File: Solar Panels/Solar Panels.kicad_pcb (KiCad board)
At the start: 2 copper layers, 113 x 82 mm, 98 parts, among them J2 5040500891

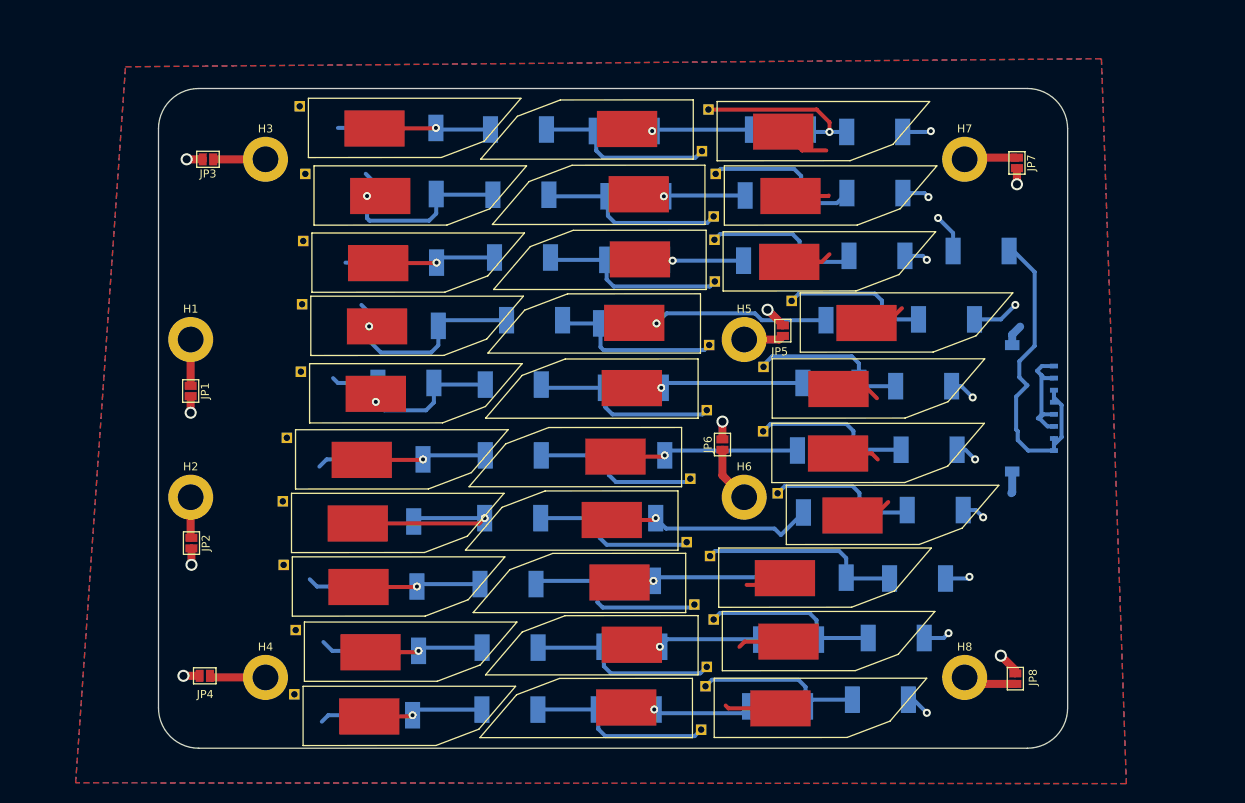
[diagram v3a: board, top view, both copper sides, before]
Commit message: Diodes changes and adjusted schematic.
Made the diode changes based off Parker's suggestions and fixed the schematic. Comments are now included within the schematic.
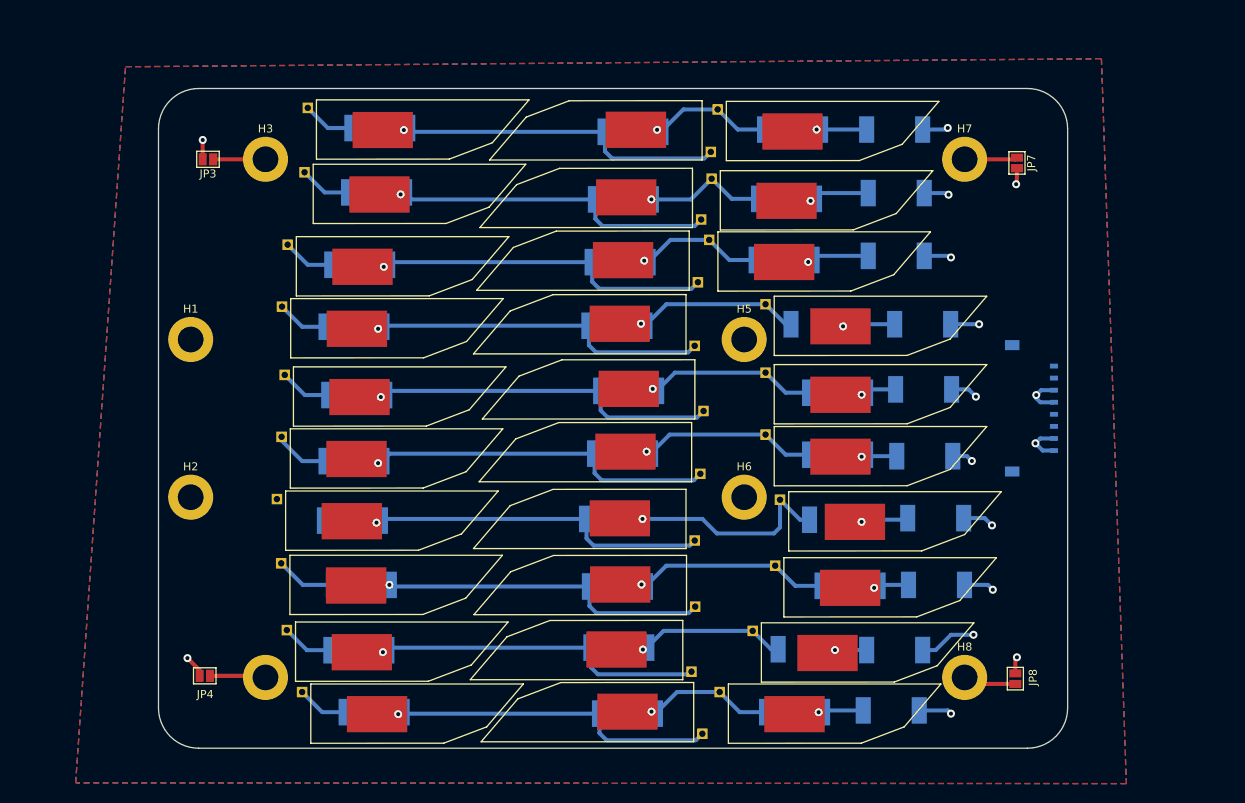
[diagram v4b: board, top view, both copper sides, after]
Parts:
- removed CR41, CR42, CR43, CR44, CR45, CR46, CR47, CR48, CR49, CR50, CR51: S3B_R1_00001, Solar Panel Library:SMC&slash_DO-214AB_PNJ
- removed JP1, JP2, JP5, JP6: Jumper_2_Open, Jumper:SolderJumper-2_P1.3mm_Open_Pad1.0x1.5mm
- H1, H2, H5, H6: value MountingHole_Pad -> MountingHole
- moved CR32 71.9 mm to (100.2, 136.7)
- moved CR16 65.6 mm to (99.3, 104.6)
- moved CR8 61.9 mm to (102.1, 87.9)
- moved CR28 59.4 mm to (99.1, 128.7)
- moved CR26 56.3 mm to (159.4, 128.6)
- moved CR25 55.1 mm to (171.6, 128.4)
- moved CR13 50.4 mm to (170.0, 104.3)
- moved CR30 44.9 mm to (161.0, 136.8)
- moved CR29 40.6 mm to (171.7, 136.7)
- moved CR27 40.0 mm to (131.7, 128.5)
- moved CR24 35.9 mm to (99.3, 121.3)
- moved CR5 34.4 mm to (153.1, 88.7)
- moved CR10 33.7 mm to (152.8, 96.3)
- moved CR9 33.2 mm to (166.7, 95.8)
- moved CR31 31.8 mm to (132.0, 136.9)
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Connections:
- CR10 pad 1: Net-(SC5--) -> Net-(SC7-+)
- CR10 pad 2: Net-(SC6-+) -> Net-(SC7--)
- CR11 pad 1: Net-(SC6-+) -> Net-(SC7--)
- CR11 pad 2: GND -> Net-(SC8--)
- CR12 pad 1: Net-(SC9-+) -> Net-(SC8--)
- CR13 pad 1: Net-(SC8--) -> +VDC
- CR13 pad 2: Net-(SC9-+) -> Net-(SC10-+)
- CR14 pad 1: Net-(SC8-+) -> Net-(SC10-+)
- CR14 pad 2: Net-(SC8--) -> Net-(SC10--)
- CR15 pad 1: Net-(SC7--) -> Net-(SC10--)
- CR15 pad 2: Net-(SC8-+) -> Net-(SC11--)
- CR16 pad 1: Net-(SC1-+) -> Net-(SC11--)
- CR16 pad 2: Net-(SC7--) -> GND
- CR17 pad 1: Net-(SC10--) -> +VDC
- CR17 pad 2: Net-(SC11-+) -> Net-(SC13-+)
- CR18 pad 1: Net-(SC11-+) -> Net-(SC13-+)
- CR18 pad 2: Net-(SC11--) -> Net-(SC13--)
- CR19 pad 1: Net-(SC11--) -> Net-(SC13--)
- CR19 pad 2: Net-(SC12-+) -> Net-(SC14--)
- CR20 pad 1: Net-(SC12-+) -> Net-(SC14--)
- CR21 pad 1: Net-(SC1-+) -> +VDC
- CR21 pad 2: Net-(SC10--) -> Net-(SC16-+)
- CR22 pad 1: Net-(SC1-+) -> Net-(SC16-+)
- CR22 pad 2: Net-(SC13--) -> Net-(SC16--)
- CR23 pad 1: Net-(SC13--) -> Net-(SC16--)
- CR23 pad 2: Net-(SC14-+) -> Net-(SC17--)
- CR24 pad 1: Net-(SC14-+) -> Net-(SC17--)
- CR24 pad 2: Net-(SC14--) -> GND
- CR25 pad 1: Net-(SC14--) -> +VDC
- CR25 pad 2: Net-(SC15-+) -> Net-(SC19-+)
- CR26 pad 1: Net-(SC15-+) -> Net-(SC19-+)
- CR26 pad 2: GND -> Net-(SC19--)
- CR27 pad 1: Net-(SC1-+) -> Net-(SC19--)
- CR27 pad 2: Net-(SC16--) -> Net-(SC20--)
- CR28 pad 1: Net-(SC16--) -> Net-(SC20--)
- CR28 pad 2: Net-(SC17-+) -> GND
- CR29 pad 1: Net-(SC17-+) -> +VDC
- CR29 pad 2: Net-(SC17--) -> Net-(SC22-+)
- CR3 pad 1: Net-(SC1--) -> +VDC
- CR3 pad 2: Net-(SC2-+) -> Net-(SC4-+)
- CR30 pad 1: Net-(SC17--) -> Net-(SC22-+)
- CR30 pad 2: Net-(SC18-+) -> Net-(SC22--)
- CR31 pad 1: Net-(SC18-+) -> Net-(SC22--)
- CR31 pad 2: GND -> Net-(SC23--)
- CR32 pad 1: Net-(SC1-+) -> Net-(SC23--)
- CR32 pad 2: Net-(SC19--) -> GND
- CR33 pad 1: Net-(SC19--) -> +VDC
- CR33 pad 2: Net-(SC20-+) -> Net-(SC25-+)
- CR34 pad 1: Net-(SC20-+) -> Net-(SC25-+)
- CR34 pad 2: Net-(SC20--) -> Net-(SC25--)
- CR35 pad 1: Net-(SC20--) -> Net-(SC25--)
- CR35 pad 2: Net-(SC21-+) -> Net-(SC26--)
- CR36 pad 1: Net-(SC21-+) -> Net-(SC26--)
- CR37 pad 1: Net-(SC1-+) -> +VDC
- CR37 pad 2: Net-(SC22--) -> Net-(SC28-+)
- CR38 pad 1: Net-(SC22--) -> Net-(SC28-+)
- CR38 pad 2: Net-(SC23-+) -> Net-(SC28--)
- CR39 pad 1: Net-(SC23-+) -> Net-(SC28--)
- CR39 pad 2: Net-(SC23--) -> Net-(SC29--)
- CR4 pad 1: Net-(SC2-+) -> Net-(SC1--)
- CR40 pad 1: Net-(SC23--) -> Net-(SC29--)
- CR40 pad 2: Net-(SC24-+) -> GND
- CR5 pad 1: Net-(SC2--) -> Net-(SC4-+)
- CR5 pad 2: Net-(SC3-+) -> Net-(SC4--)
- CR6 pad 1: Net-(SC3-+) -> Net-(SC2--)
- CR7 pad 2: Net-(SC5-+) -> Net-(SC5--)
- CR8 pad 1: Net-(SC1-+) -> Net-(SC5--)
- CR8 pad 2: Net-(SC4--) -> GND
- CR9 pad 1: Net-(SC5-+) -> +VDC
- CR9 pad 2: Net-(SC5--) -> Net-(SC7-+)
- H1 pad 1: Net-(JP1-A) -> (no net)
- H2 pad 1: Net-(JP2-A) -> (no net)
- H5 pad 1: Net-(JP5-A) -> (no net)
- H6 pad 1: Net-(JP6-A) -> (no net)
- SC10 pad 1: Net-(SC1-+) -> Net-(SC10-+)
- SC11 pad 1: Net-(SC11-+) -> Net-(SC10--)
- SC12 pad 1: Net-(SC12-+) -> Net-(SC11--)
- SC13 pad 1: Net-(SC1-+) -> Net-(SC13-+)
- SC14 pad 1: Net-(SC14-+) -> Net-(SC13--)
- SC15 pad 1: Net-(SC15-+) -> Net-(SC14--)
- SC16 pad 1: Net-(SC1-+) -> Net-(SC16-+)
- SC17 pad 1: Net-(SC17-+) -> Net-(SC16--)
- SC18 pad 1: Net-(SC18-+) -> Net-(SC17--)
- SC19 pad 1: Net-(SC1-+) -> Net-(SC19-+)
- SC2 pad 1: Net-(SC2-+) -> Net-(SC1--)
- SC20 pad 1: Net-(SC20-+) -> Net-(SC19--)
- SC21 pad 1: Net-(SC21-+) -> Net-(SC20--)
- SC22 pad 1: Net-(SC1-+) -> Net-(SC22-+)
- SC23 pad 1: Net-(SC23-+) -> Net-(SC22--)
- SC24 pad 1: Net-(SC24-+) -> Net-(SC23--)
- SC25 pad 1: Net-(SC1-+) -> Net-(SC25-+)
- SC26 pad 1: Net-(SC26-+) -> Net-(SC25--)
- SC27 pad 1: Net-(SC27-+) -> Net-(SC26--)
- SC28 pad 1: Net-(SC1-+) -> Net-(SC28-+)
- SC29 pad 1: Net-(SC29-+) -> Net-(SC28--)
- SC3 pad 1: Net-(SC3-+) -> Net-(SC2--)
- SC30 pad 1: Net-(SC30-+) -> Net-(SC29--)
- SC4 pad 1: Net-(SC1-+) -> Net-(SC4-+)
- SC5 pad 1: Net-(SC5-+) -> Net-(SC4--)
- SC6 pad 1: Net-(SC6-+) -> Net-(SC5--)
- SC7 pad 1: Net-(SC1-+) -> Net-(SC7-+)
- SC8 pad 1: Net-(SC8-+) -> Net-(SC7--)
- SC9 pad 1: Net-(SC9-+) -> Net-(SC8--)
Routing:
- net Net-(SC1-+): track 94.5 -> 6.22 mm, vias 11 -> 1
- net Net-(SC20-+): track 26.0 -> 0.00 mm, vias 1 -> 0
- net Net-(SC21-+): track 25.0 -> 0.00 mm, vias 1 -> 0
- net Net-(SC11-+): track 24.7 -> 0.00 mm, vias 1 -> 0
- net Net-(SC17-+): track 22.9 -> 0.00 mm, vias 1 -> 0
- net Net-(SC12-+): track 22.6 -> 0.00 mm, vias 1 -> 0
- net Net-(SC23--): track 22.9 -> 45.4 mm, vias 0 -> 1
- net Net-(SC17--): track 21.5 -> 43.7 mm, vias 0 -> 1
- net Net-(SC20--): track 21.1 -> 42.8 mm, vias 0 -> 1
- net Net-(SC14-+): track 21.5 -> 0.00 mm, vias 1 -> 0
- net Net-(SC23-+): track 21.5 -> 0.00 mm, vias 1 -> 0
- net Net-(SC6-+): track 21.4 -> 0.00 mm, vias 1 -> 0
- net Net-(SC11--): track 21.7 -> 42.6 mm, vias 0 -> 1
- net Net-(SC14--): track 23.7 -> 43.6 mm, vias 0 -> 1
- net Net-(SC2--): track 22.5 -> 41.6 mm, vias 0 -> 1
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- added copper zone on F.Cu, net +VDC
- removed copper zone on F.Cu, net Net-(SC1-+)

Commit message: Quick Adjustments to Schematic and Routing
Adjusted so there's only one bypass diode for the entire panel. Made changes to the routing as well.
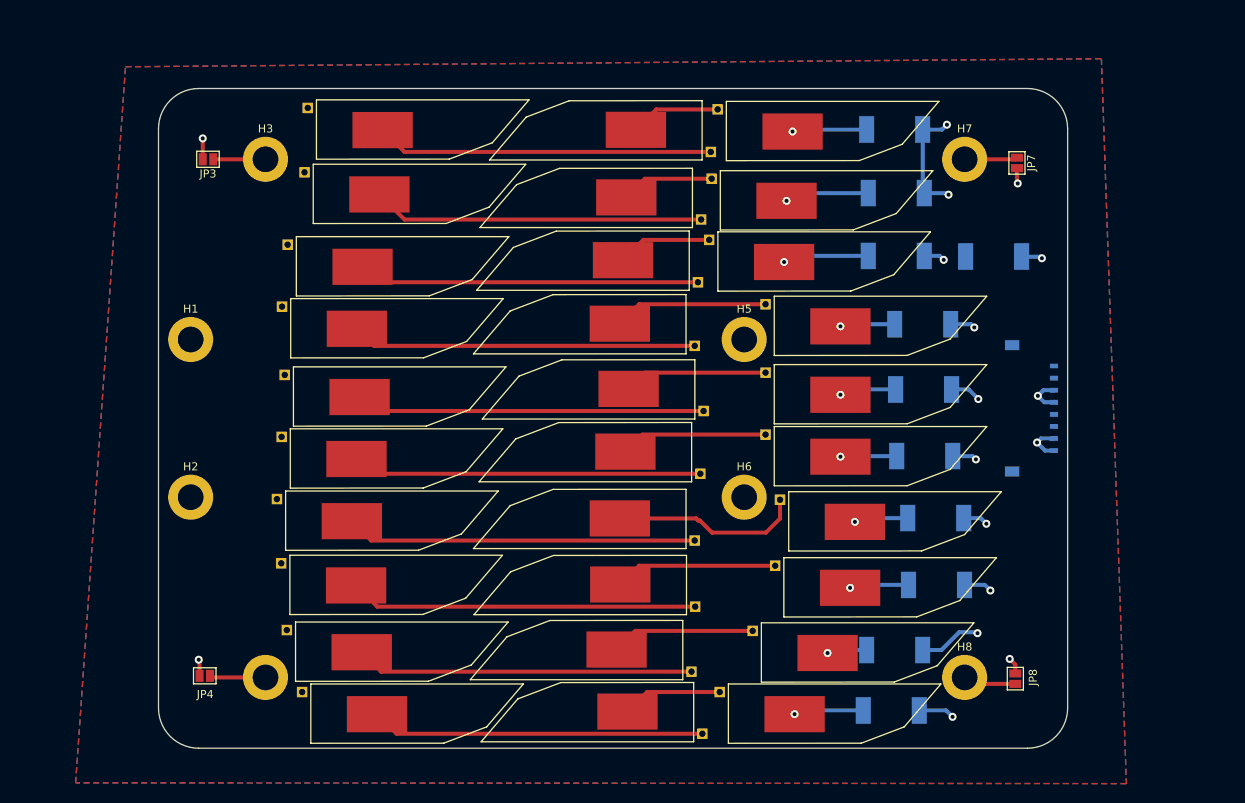
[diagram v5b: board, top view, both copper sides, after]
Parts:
- removed CR10, CR11, CR12, CR14, CR15, CR16, CR18, CR19, CR20, CR22, CR23, CR24, CR26, CR27, CR28, CR30, CR31, CR32, CR34, CR35, CR36, CR38, CR39, CR4, CR40, CR5, CR6, CR7, CR8: S3B_R1_00001, Solar Panel Library:SMC&slash_DO-214AB_PNJ
- moved CR2 29.6 mm to (178.8, 95.9)
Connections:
- CR2 pad 1: Net-(SC1-+) -> +VDC
- CR2 pad 2: Net-(SC1--) -> GND
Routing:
- net GND: track 69.0 -> 8.67 mm
- net +VDC: track 48.8 -> 57.9 mm, vias 12 -> 13
- net Net-(SC4--): track 18.6 -> 11.6 mm, vias 1 -> 0
- net Net-(SC7--): track 18.3 -> 11.8 mm, vias 1 -> 0
- net Net-(SC19--): track 29.1 -> 23.7 mm, vias 1 -> 0
- net Net-(SC22--): track 24.7 -> 20.2 mm, vias 1 -> 0
- net Net-(SC1--): track 15.7 -> 11.2 mm, vias 1 -> 0
- net Net-(SC16--): track 22.4 -> 18.3 mm, vias 1 -> 0
- net Net-(SC28--): track 16.6 -> 12.5 mm, vias 1 -> 0
- net Net-(SC13--): track 21.6 -> 17.9 mm, vias 1 -> 0
- net Net-(SC1-+): track 6.22 -> 9.31 mm
- net Net-(SC28-+): track 5.64 -> 8.73 mm
- net Net-(SC7-+): track 7.79 -> 10.8 mm
- net Net-(SC22-+): track 4.42 -> 7.41 mm
- net Net-(SC4-+): track 7.57 -> 10.6 mm
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
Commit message: Routed the PCB after the Footprint Adjustments
Routed the PCB after making adjustments to the TriSolX footprint.
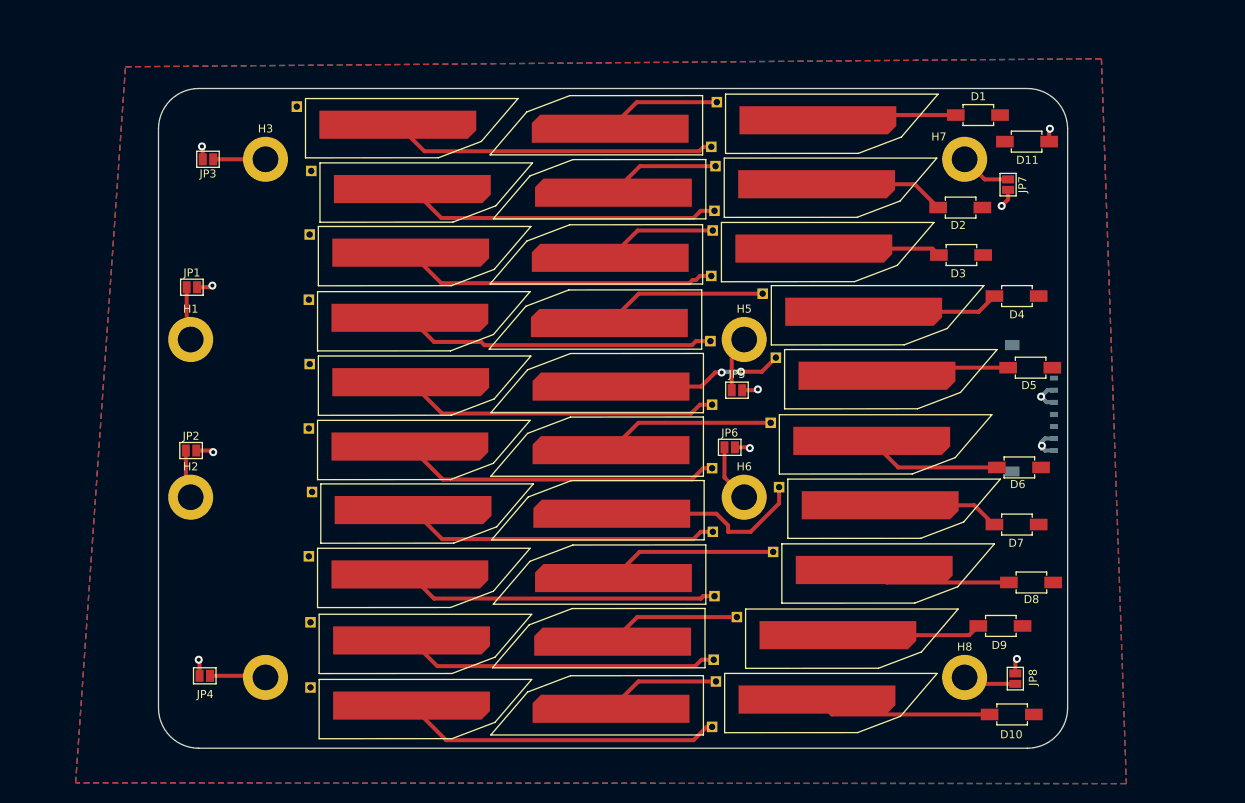
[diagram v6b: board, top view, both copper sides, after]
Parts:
- removed CR1, CR13, CR17, CR2, CR21, CR25, CR29, CR3, CR33, CR37, CR9: S3B_R1_00001, Solar Panel Library:SMC&slash_DO-214AB_PNJ
- added D1: PMEG10020AELPX, Solar Panel Library:PMEG10020AELPX, F.Cu at (176.9, 78.3)
- added D10: PMEG10020AELPX, Solar Panel Library:PMEG10020AELPX, F.Cu at (181.1, 152.8)
- added D11: PMEG10020AELPX, Solar Panel Library:PMEG10020AELPX, F.Cu at (182.9, 81.6)
- added D2: PMEG10020AELPX, Solar Panel Library:PMEG10020AELPX, F.Cu at (174.7, 89.8)
- added D3: PMEG10020AELPX, Solar Panel Library:PMEG10020AELPX, F.Cu at (174.8, 95.7)
- added D4: PMEG10020AELPX, Solar Panel Library:PMEG10020AELPX, F.Cu at (181.7, 100.8)
- added D5: PMEG10020AELPX, Solar Panel Library:PMEG10020AELPX, F.Cu at (183.4, 109.7)
- added D6: PMEG10020AELPX, Solar Panel Library:PMEG10020AELPX, F.Cu at (182.0, 122.1)
- added D7: PMEG10020AELPX, Solar Panel Library:PMEG10020AELPX, F.Cu at (181.7, 129.2)
- added D8: PMEG10020AELPX, Solar Panel Library:PMEG10020AELPX, F.Cu at (183.5, 136.4)
- added D9: PMEG10020AELPX, Solar Panel Library:PMEG10020AELPX, F.Cu at (179.7, 141.8)
- added JP1: Jumper_2_Open, Jumper:SolderJumper-2_P1.3mm_Open_Pad1.0x1.5mm, F.Cu at (79.2, 99.7)
- added JP2: Jumper_2_Open, Jumper:SolderJumper-2_P1.3mm_Open_Pad1.0x1.5mm, F.Cu at (79.0, 120.0)
- added JP5: Jumper_2_Open, Jumper:SolderJumper-2_P1.3mm_Open_Pad1.0x1.5mm, F.Cu at (146.9, 112.5)
- added JP6: Jumper_2_Open, Jumper:SolderJumper-2_P1.3mm_Open_Pad1.0x1.5mm, F.Cu at (146.0, 119.6)
- H1, H2, H5, H6: value MountingHole -> MountingHole_Pad
- moved SC21 4.46 mm to (103.4, 127.7)
- moved SC18 3.55 mm to (103.0, 119.8)
- moved SC24 3.55 mm to (103.0, 135.7)
- moved SC12 3.45 mm to (103.0, 103.8)
- moved SC15 3.38 mm to (103.1, 111.8)
- moved SC26 3.14 mm to (134.7, 143.5)
- moved SC27 3.09 mm to (103.2, 143.8)
- moved SC9 3.02 mm to (103.1, 95.7)
- moved JP7 2.92 mm to (180.6, 87.0)
- moved SC23 2.73 mm to (134.8, 135.6)
- moved SC25 2.61 mm to (156.2, 143.2)
- moved SC20 2.50 mm to (134.6, 127.6)
- moved SC13 2.27 mm to (161.1, 111.0)
- moved SC11 2.04 mm to (134.3, 103.9)
- moved SC5 1.98 mm to (134.8, 87.7)
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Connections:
- H1 pad 1: (no net) -> Net-(JP1-A)
- H2 pad 1: (no net) -> Net-(JP2-A)
- H5 pad 1: (no net) -> Net-(JP5-A)
- H6 pad 1: (no net) -> Net-(JP6-A)
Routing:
- net +VDC: track 57.9 -> 8.05 mm, vias 13 -> 2
- net Net-(SC28-+): track 8.73 -> 22.2 mm, vias 1 -> 0
- net Net-(SC25-+): track 5.01 -> 17.9 mm, vias 1 -> 0
- net Net-(SC10-+): track 6.85 -> 17.1 mm, vias 1 -> 0
- net Net-(SC22-+): track 7.41 -> 17.4 mm, vias 1 -> 0
- net Net-(SC16-+): track 7.03 -> 16.9 mm, vias 1 -> 0
- net Net-(SC13-+): track 7.13 -> 16.7 mm, vias 1 -> 0
- net GND: track 8.67 -> 17.6 mm, vias 4 -> 9
- net Net-(SC19-+): track 6.75 -> 15.2 mm, vias 1 -> 0
- net Net-(SC1-+): track 9.31 -> 17.4 mm, vias 1 -> 0
- net Net-(JP6-A): track 0.00 -> 7.21 mm
- net Net-(JP5-A): track 0.00 -> 6.94 mm
- net Net-(JP1-A): track 0.00 -> 6.71 mm
- net Net-(JP2-A): track 0.00 -> 6.05 mm
- net Net-(SC4-+): track 10.6 -> 16.3 mm, vias 1 -> 0
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
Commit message: Refined Simons 2u
I tried refining Simons design a bit and aligned the holes/dimensions to the most current frame version.

Looking good on the structural side. Think we just need a last electrical review then should be ready to order.
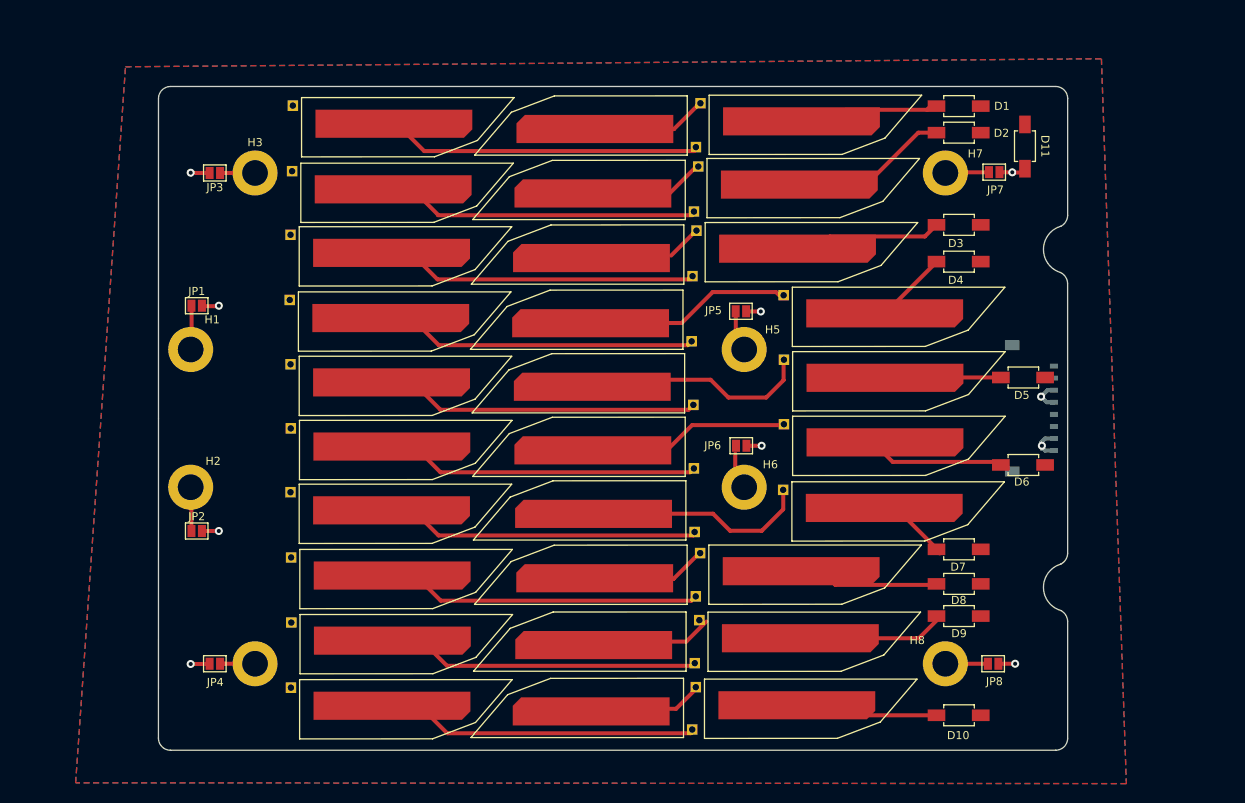
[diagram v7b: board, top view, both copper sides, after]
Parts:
- moved JP2 10.0 mm to (79.8, 130.0)
- moved JP5 9.82 mm to (147.4, 102.7)
- moved D2 9.31 mm to (174.5, 80.5)
- moved SC22 9.08 mm to (151.6, 135.2)
- moved D8 9.00 mm to (174.5, 136.6)
- moved D4 8.38 mm to (174.5, 96.5)
- moved D7 7.83 mm to (174.5, 132.3)
- moved D10 6.60 mm to (174.5, 152.9)
- moved D9 5.34 mm to (174.5, 140.6)
- moved SC25 4.68 mm to (151.5, 143.6)
- moved D3 3.77 mm to (174.5, 91.9)
- moved JP8 3.32 mm to (178.7, 146.5), turned to 0 degrees
- moved H7 2.94 mm to (172.8, 85.5)
- moved H8 2.94 mm to (172.8, 146.5)
- moved SC21 2.69 mm to (100.7, 127.7)
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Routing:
- net Net-(SC28-+): track 22.2 -> 10.9 mm
- net Net-(SC7--): track 14.1 -> 4.37 mm
- net Net-(SC4--): track 14.1 -> 4.82 mm
- net Net-(SC22--): track 21.2 -> 12.2 mm
- net Net-(SC10-+): track 17.1 -> 11.2 mm
- net Net-(SC16--): track 21.2 -> 15.7 mm
- net Net-(SC19-+): track 15.2 -> 10.0 mm
- net Net-(SC29--): track 39.8 -> 35.1 mm
- net Net-(SC26--): track 39.2 -> 34.7 mm
- net Net-(SC10--): track 20.6 -> 16.2 mm
- net Net-(SC1-+): track 17.4 -> 13.3 mm
- net Net-(SC25--): track 16.7 -> 12.7 mm
- net Net-(JP1-A): track 6.71 -> 3.07 mm
- net Net-(JP4-A): track 6.98 -> 3.39 mm
- net Net-(SC13-+): track 16.7 -> 13.4 mm
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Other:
- board size 113 x 82 mm -> 113 x 82.5 mm
